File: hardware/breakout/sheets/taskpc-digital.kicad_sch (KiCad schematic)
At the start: 63 parts, among them J2 Connector 0 (analog + AISENSE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, J3 Connector 1 (digital, task PC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, J4 Manual reward button (panel), J5 Remote reward jack (parallel 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, J6 Reward driver out (BNC, place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, U10 SN74HCT541PW, U11 SN74HCT541PW, U12 SN74HCT32D, U13 SN74HCT14D, U5 SN74LVC541APW, U6 SN74LVC541APW, U7 SN74LVC541APW, U8 SN74HCT541PW, U9 SN74HCT541PW

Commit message: fix(hw): reward-OR polarity, sourced MDR68/connector-0 pinouts
Task 8 fix round 1 -- three findings from review, all this task's own
disclosed concerns the review was right to raise.

Finding 1 (CRITICAL): the reward-OR debounce stage placed a 74HCT14
Schmitt PAIR, exactly as task-8-brief.md's own (wrong) literal text
specified. Two series inversions cancel, so the debounced button idled
HIGH into an OR gate against an active-HIGH RWD_CMD -- RWD_DLVR would
have asserted continuously (reward driver stuck open, "delivered"
stuck true in every recording). Fixed to a single Schmitt inversion
(place_debounce_inverter(), was place_debounce_inverters()):
idle-LOW/active-HIGH, matching what an OR combination with an
active-HIGH RWD_CMD actually needs. RWD_CMD's assumed active-HIGH
polarity is now stated explicitly on-sheet. Checker gained a
same-polarity structural check (debounce IC pin 1->2, one hop, not a
two-hop path through a middle net) plus a negative control simulating
the pair being reintroduced.

Finding 2: Connector 1's physical MDR68 pin assignment was this
sheet's own sequential guess. Now sourced from NI's own "X Series User
Manual" (370784K-01, May 2019), Figure A-5 "NI PCIe-6323/6343 Pinout"
-- the task PC's own card -- for every P0.x and D GND position,
cross-checked by two independent parses of the source PDF that agreed
exactly before either was used. All 12 real D GND pins are now tied
(was an arbitrary 2, one of which is actually an analog AI GND pin in
the real table).

Finding 3: Connector 0's 9 task-PC analog channels (A_EYE_LX_TPC etc,
sourced from plan.md's own net-naming table and Task 10 Step 3, not
invented) and its AISENSE-to-AGND tie are now wired on this sheet,
since only the file that places a symbol can label its pins and Task
10 does not exist yet. Physical AI-channel pins sourced from the same
NI manual/figure as Finding 2.

Verification: kicad-cli sch erc 0 errors, 46 warnings (all
isolated_pin_label, the same accepted class as before --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
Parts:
- J2: value Connector 0 (analog + AISENSE, task PC NI) -- reserved for Task 10 -> Connector 0 (analog + AISENSE, task PC NI)
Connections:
- net ACC_TRIG_TPC: now also J3.40; no longer J3.22
- net DGND: now also J3.12, J3.13, J3.15, J3.18, J3.35, J3.36, J3.4, J3.44, J3.50, J3.53, J3.7, J3.9, U13.3; no longer J3.24, J3.25
- net EVT_D0_TPC: now also J3.52; no longer J3.1
- net EVT_D10_TPC: now also J3.43; no longer J3.11
- net EVT_D11_TPC: now also J3.42; no longer J3.12
- net EVT_D12_TPC: now also J3.41; no longer J3.13
- net EVT_D13_TPC: now also J3.6; no longer J3.14
- net EVT_D14_TPC: now also J3.5; no longer J3.15
- net EVT_D15_TPC: now also J3.38; no longer J3.16
- net EVT_D1_TPC: now also J3.17; no longer J3.2
- net EVT_D2_TPC: now also J3.49; no longer J3.3
- net EVT_D3_TPC: now also J3.47; no longer J3.4
- net EVT_D4_TPC: now also J3.19; no longer J3.5
- net EVT_D5_TPC: now also J3.51; no longer J3.6
- net EVT_D6_TPC: now also J3.16; no longer J3.7
- net EVT_D7_TPC: now also J3.48; no longer J3.8
- net EVT_D8_TPC: now also J3.11; no longer J3.9
- net EVT_STROBE_TPC: now also J3.37; no longer J3.17
- net PD1_COMP_TPC: now also J3.46; no longer J3.20
- net PD2_COMP_TPC: now also J3.2; no longer J3.21
- net RHS_STIM_OUT_TPC: now also J3.1; no longer J3.23
- net RWD_BTN_DEB: now also U13.2; no longer U13.4
- net RWD_CMD_TPC: now also J3.3; no longer J3.18
- net STIM_TRIG_TPC: now also J3.45; no longer J3.19
- net A_MISC1_TPC: now reaches J2.25
- net A_JOY_X_TPC: now reaches J2.28
- net A_EYE_RY_TPC: now reaches J2.30
- net A_EYE_LY_TPC: now reaches J2.33
- net A_MISC3_TPC: now reaches J2.34
- net A_MISC2_TPC: now reaches J2.57
- net A_JOY_Y_TPC: now reaches J2.60
- net AGND: now reaches J2.62
- net A_EYE_RX_TPC: now reaches J2.65
- net A_EYE_LX_TPC: now reaches J2.68
- removed net RWD_BTN_INV1: U13.2, U13.3
- no-connect marks 132 -> 113
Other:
- note added: ""NI PCIe-6323/6343 Pinout", same source as Connector 1 below -- see this"
- note added: "(fix round 1, finding 3); Task 10 drives these SAME contract net names from its"
- note added: "74HCT14 Schmitt inverter (NOT a pair -- a pair was this task's own pre-fix-"
- note added: "AI0=pin68=A_EYE_LX_TPC AI1=pin33=A_EYE_LY_TPC AI2=pin65=A_EYE_RX_TPC"
- note added: "AI3=pin30=A_EYE_RY_TPC AI4=pin28=A_JOY_X_TPC AI5=pin60=A_JOY_Y_TPC"
- note added: "AI6=pin25=A_MISC1_TPC AI7=pin57=A_MISC2_TPC AI8=pin34=A_MISC3_TPC"
- note added: "AISENSE=pin62 -> AGND (NRSE reference -- spec Decision 5; the easiest wire on"
- note added: "Connector 0 (analog + AISENSE): 9 task-PC analog channels + AISENSE wired here"
- note added: "LOW input regardless of the button side's own inverter count."
- note added: "MonkeyLogic before commissioning: if active-HIGH as assumed, this OR gate is"
- note added: "MonkeyLogic side independently. VERIFY RWD_CMD's actual polarity against"
- note added: "ORed with an active-HIGH RWD_CMD asserts RWD_DLVR permanently) inverts ONCE,"
- note added: "P0.12=pin19 P0.13=pin51 P0.14=pin16 P0.15=pin48 P0.16=pin11 P0.17=pin10"
- note added: "P0.18=pin43 P0.19=pin42 P0.20=pin41 P0.21=pin6 P0.22=pin5 P0.23=pin38"
- note added: "P0.24=pin37(STROBE) P0.25=pin3(RWD_CMD) P0.26=pin45(STIM_TRIG)"
- note added: "P0.27=pin46(PD1_COMP) P0.28=pin2(PD2_COMP) P0.29=pin40(ACC_TRIG)"
- note added: "P0.30=pin1(RHS_STIM_OUT) P0.31=pin39 (spare, no_connect). D GND (all 12 real"
- note added: "PCIe-6323/6343 Pinout": P0.8=pin52 P0.9=pin17 P0.10=pin49 P0.11=pin47"
- note added: "Physical MDR68 pin per P0.x line is SOURCED (fix round 1, finding 2), not"
- note added: "Physical pins sourced from NI's X Series User Manual (370784K-01), Figure A-5"
- note added: "RWD_BTN idles HIGH (10k pull-up to +5V), reads LOW while pressed. A SINGLE"
- note added: "RWD_CMD polarity is ASSUMED ACTIVE-HIGH (idle-LOW, pulses HIGH on delivery --"
- note added: "Remaining 58 pins (spare AI9-15, P0.0-7/P1.0-7/P2.x, D GND, +5V, AO*, NC) stay"
- note added: "Reward OR polarity (fix round 1, finding 1 -- CRITICAL, corrected here):"
- note added: "See this generator's own MDR1_PIN_BY_P0/MDR1_DGND_PINS and"
- note added: "clamp circuitry lives on THIS sheet, only the labelled connection point does."
- note added: "correct; an OR gate cannot correctly combine one active-HIGH and one active-"
- note added: "docstring."
- note added: "generator's own MDR0_AI_PIN/MDR0_AISENSE_PIN and task-8-report.md "Fix round 1"."
- note added: "invert): stated explicitly because this sheet cannot verify the task PC/"
- note added: "no_connect: outside this task's own contract -- see _place_connector0()'s own"
- note added: "own front-end/buffer outputs (plan.md Task 10 Step 3) -- no buffer/series-R/"
- note added: "pins tied, not an arbitrary 2): 4,7,9,12,13,15,18,35,36,44,50,53."
- note added: "round-1 defect: 2 series stages cancel, leaving RWD_BTN_DEB idle-HIGH, which"
- note added: "sequential -- NI's own X Series User Manual (370784K-01), Figure A-5 "NI"
- note added: "so RWD_BTN_DEB idles LOW and reads HIGH while pressed -- active-HIGH."
- note added: "task-8-report.md "Fix round 1" for the full retrieval/cross-check method."
- note added: "this board to omit by accident, so check_taskpc_digital_netlist.py asserts it)."
- note added: "this design's other event lines' own convention, and SN74LVC541APW does not"
- note removed: "A_MISC1/2/3, spec Sec.3.2) onto this same JJ2 instance."
- note removed: "Connector 0 (analog + AISENSE): placed here, left fully unpopulated."
- note removed: "HIGH (this design's other event lines' convention, and SN74LVC541APW does not"
- note removed: "PD2_COMP,ACC_TRIG,RHS_STIM_OUT) -- this board's OWN choice, not yet confirmed"
- note removed: "RWD_BTN_DEB also reads LOW while pressed. RWD_CMD is assumed idle-LOW/pulse-"
- note removed: "Reward OR polarity: RWD_BTN idles HIGH (10k pull-up to +5V), reads LOW while"
- note removed: "Task 10 wires the 9 task-PC analog channels (A_EYE_LX/LY/RX/RY, A_JOY_X/Y,"
- note removed: "This sheet assigns Connector 1's own physical MDR68 pins 1-23 SEQUENTIALLY to"
- note removed: "against NI's SCSI/MDR pin-position diagram for the real SHC68-68-EPM cable;"
- note removed: "commissioning: if RWD_CMD is active-HIGH as assumed, this OR gate is correct;"
- note removed: "continuously instead of pulsing on delivery."
- note removed: "if RWD_CMD instead turns out active-LOW, RWD_DLVR would read HIGH almost"
- note removed: "invert). VERIFY RWD_CMD's actual polarity against MonkeyLogic before"
- note removed: "pin18=P0.25/RWD_CMD, pin19=P0.26/STIM_TRIG, pin20-23=P0.27-30/PD1_COMP,"
- note removed: "pressed. The 74HCT14 pair is NON-inverting (2 series Schmitt stages), so"
- note removed: "see this generator's own _place_connector1() docstring."
- note removed: "these 23 lines (pin1=P0.8/EVT_D0 ... pin16=P0.23/EVT_D15, pin17=P0.24/STROBE,"

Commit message: fix(hw): retire taskpc-digital's stale PD1_COMP/PD2_COMP/ACC_TRIG PWR_FLAGs
Task 8's own outbound buffer placed a PWR_FLAG on each of PD1_COMP/
PD2_COMP/ACC_TRIG/RHS_STIM_OUT because nothing drove them yet, and its own
docstring already instructed deleting each one "the moment their own real
driving pin is wired to it" -- comparators.kicad_sch now does exactly that
for the first three (an LM339 open_collector output on each), so their own
flags are deleted here, exactly as instructed. Left in place, a PWR_FLAG on
the same net as an open_collector driver trips ERC's pin_to_pin rule
("Pins of type Open collector and Power output are connected") -- confirmed
empirically: 4 errors before this fix, 0 after. RHS_STIM_OUT's own flag
stays; Task 11 (opto-intan) hasn't wired its own driver yet.

Co-Authored-By: Claude Opus 5 (1M context) <noreply@anthropic.com>
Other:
- note added: "PD1_COMP/PD2_COMP/ACC_TRIG's own PWR_FLAGs (formerly here too) were deleted at"
- note added: "RHS_STIM_OUT: the one remaining PWR_FLAG to the left of U7 is TEMPORARY -- it"
- note added: "Task 10d (comparators.kicad_sch), which gave all three a real open_collector"
- note added: "driver -- task-10d-report.md."
- note added: "exists only because Task 11 (opto-intan) has not been built yet. DELETE it"
- note added: "left in place, a PWR_FLAG trips ERC's pin_to_pin rule against a driving pin on"
- note added: "the moment its own real driver (an optocoupler output) is wired to that net --"
- note added: "the same net (confirmed empirically, see _place_outbound()'s own docstring)."
- note removed: "(LM339 open_collector output / optocoupler output) is wired to that net --"
- note removed: "PD1_COMP/PD2_COMP/ACC_TRIG/RHS_STIM_OUT: the 4 PWR_FLAGs to the left of U7 are"
- note removed: "TEMPORARY -- they exist only because Task 10 (comparators) and Task 11 (opto-"
- note removed: "_place_outbound()'s own docstring in gen_breakout_taskpc_digital.py)."
- note removed: "intan) have not been built yet. DELETE each one the moment its own real driver"
- note removed: "left in place, a PWR_FLAG trips ERC's pin_to_pin rule against an"
- note removed: "open_collector driver on the same net (confirmed empirically, see"

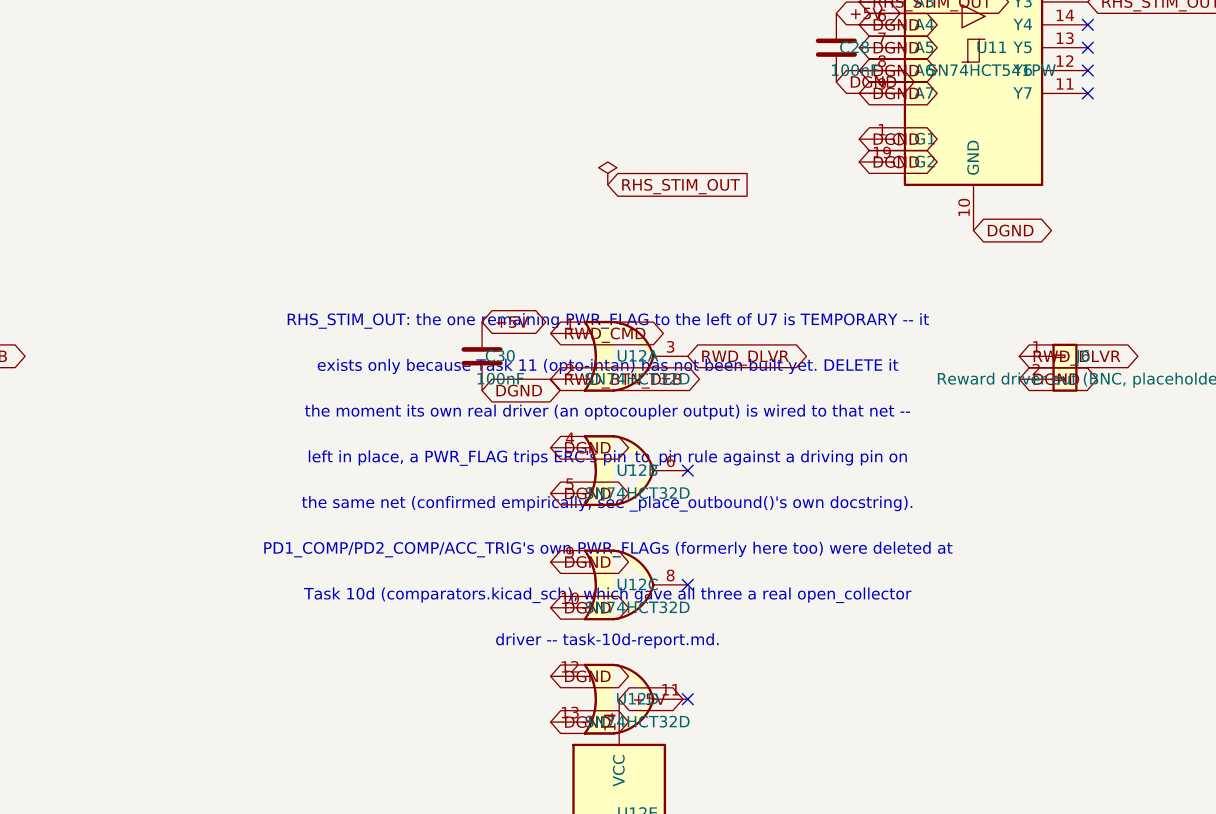
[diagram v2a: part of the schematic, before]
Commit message: feat(hw): opto-intan sheet -- 6 isolated digital channels, ACSL-6420
One Broadcom ACSL-6400 (4 outbound: strobe, barcode, RWD_CMD, RWD_DLVR)
plus one ACSL-6420 (quad, bi-directional 2/2 -- NOT a second ACSL-6400)
carry the barrier between DGND and INTAN_GND. The ACSL-6420 substitution
is a correction this task's own pin-by-pin datasheet verification found:
an all-in-one part's four channels share one VDD/GND on the output side,
and this sheet's second package needs one outbound channel (STIM_TRIG)
and one inbound channel (RHS_STIM_OUT) simultaneously -- opposite
directions an all-in-one part cannot provide without putting a channel's
output on the wrong side of the barrier. ACSL-6420's 2/2 split is built
for exactly this; the unused channel of each direction is a genuine
spare. Total across both opto sheets: 7xACSL-6400 + 1xACSL-6420 = eight
quad packages, 30 channels.

RHS_STIM_OUT's own inbound path (the one signal originating inside the
Intan domain) gets the same series-R + BAT54S clamp protection every
other panel input on this board carries, referenced to a new ISO_5V
rail (LD1117S50TR_SOT223 regulating ISO_P12 down to 5V -- ISO_P12/N12
are +-12V, too high for the ACSL family's 5.5V absolute max VDD).

Cross-sheet consequences bundled into this commit: taskpc-digital's own
temporary PWR_FLAG on RHS_STIM_OUT (Task 8) is deleted now that this
sheet gives it a real driver; check_breakout_pi_interface_netlist.py's
BARCODE_PI fan-out count moves 6->7; check_breakout_power_netlist.py's
+5V/DGND bypass count moves 9->10 (the ACSL-6420's own VDD1/GND1 pair).

check_breakout_opto_ni_netlist.py's own domain-disjointness and package-
identity checks are also fixed here: ACSL-6400 is now a SHARED part
value across both opto sheets, so a project-wide Value/rail scan pulled
in opto-intan's own package (and, before scoping to each sheet's own
components, mux-intan's and power's own already-reviewed straddling
parts too). Both checkers now discover "this sheet's own component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
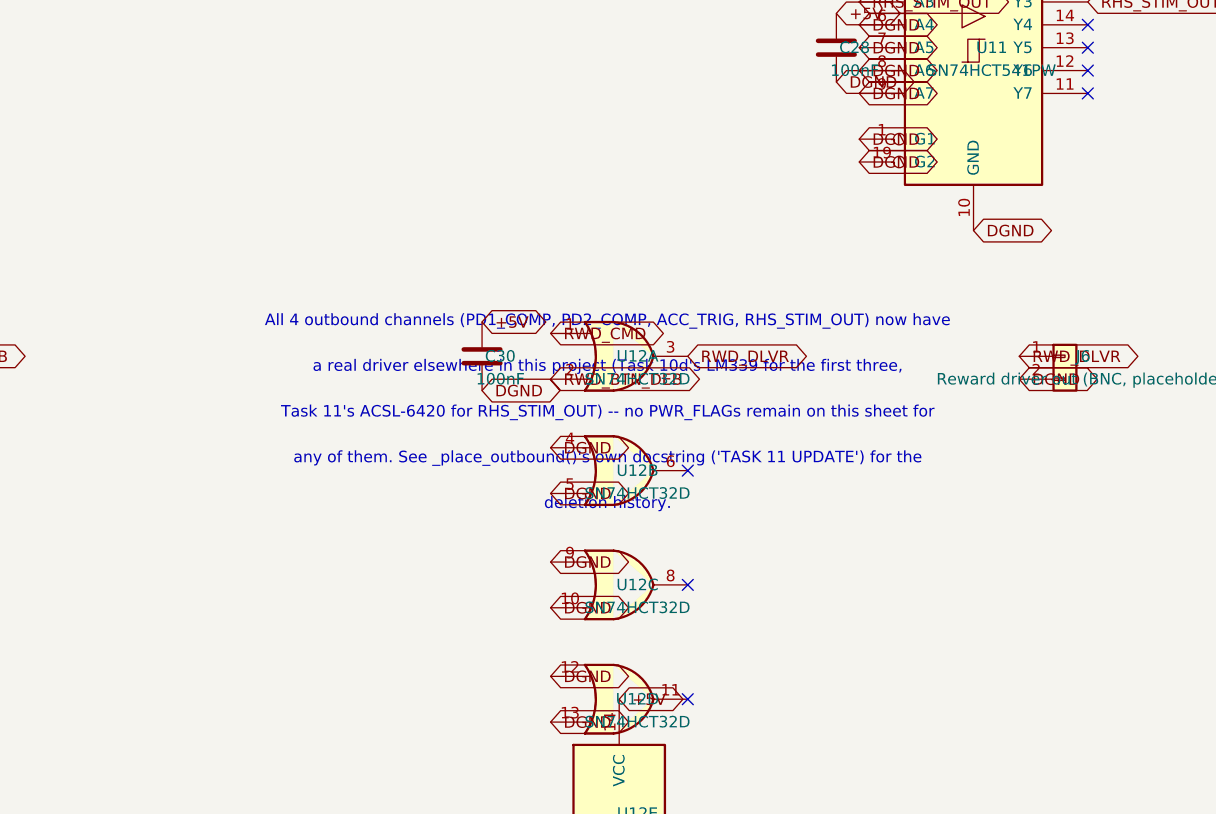
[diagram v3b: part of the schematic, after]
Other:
- note added: "All 4 outbound channels (PD1_COMP, PD2_COMP, ACC_TRIG, RHS_STIM_OUT) now have"
- note added: "Task 11's ACSL-6420 for RHS_STIM_OUT) -- no PWR_FLAGs remain on this sheet for"
- note added: "a real driver elsewhere in this project (Task 10d's LM339 for the first three,"
- note added: "any of them. See _place_outbound()'s own docstring ('TASK 11 UPDATE') for the"
- note added: "deletion history."
- note removed: "PD1_COMP/PD2_COMP/ACC_TRIG's own PWR_FLAGs (formerly here too) were deleted at"
- note removed: "RHS_STIM_OUT: the one remaining PWR_FLAG to the left of U7 is TEMPORARY -- it"
- note removed: "Task 10d (comparators.kicad_sch), which gave all three a real open_collector"
- note removed: "driver -- task-10d-report.md."
- note removed: "exists only because Task 11 (opto-intan) has not been built yet. DELETE it"
- note removed: "left in place, a PWR_FLAG trips ERC's pin_to_pin rule against a driving pin on"
- note removed: "the moment its own real driver (an optocoupler output) is wired to that net --"
- note removed: "the same net (confirmed empirically, see _place_outbound()'s own docstring)."
